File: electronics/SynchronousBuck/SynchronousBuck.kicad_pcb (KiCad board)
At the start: 4 copper layers, 90 x 81 mm, 58 parts, among them J101 Conn_01x02, J102 Conn_01x04_Male, J103 Conn_01x02, J104 Conn_01x02, Q101 BSC070N10NS5, Q102 BSC067N06LS3G, U101 LM5116MH

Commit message: Updated layout and schematic. Added zener diodes to protect output of measurements
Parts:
- removed R102, R109, R110: 1k2, Resistor_SMD:R_0603_1608Metric
- added D102: 5V1, Diode_SMD:D_SOD-123, F.Cu at (126.7, 107.5)
- added D103: 5V1, Diode_SMD:D_SOD-123, F.Cu at (124.3, 97.2)
- added R120: 24k, Resistor_SMD:R_0603_1608Metric, F.Cu at (118.2, 104.0)
- R101: value 24k -> 18k
- moved R101 12.5 mm to (109.1, 121.3)
- turned R111 to 180 degrees
- turned C116 to 270 degrees
- turned C117 to 270 degrees
- turned C120 to 180 degrees
- turned C121 to 90 degrees
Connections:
- C116 pad 1: GND -> /VOUT
- C116 pad 2: /VOUT -> GND
- C117 pad 1: GND -> /VOUT
- C117 pad 2: /VOUT -> GND
- C120 pad 1: GND -> VCC
- C120 pad 2: VCC -> GND
- C121 pad 1: GND -> VCC
- C121 pad 2: VCC -> GND
- R101 pad 1: VCC -> Net-(R101-Pad1)
- R101 pad 2: Net-(R101-Pad2) -> VCC
- R111 pad 1: Net-(R102-Pad2) -> GND
- R111 pad 2: GND -> Net-(R101-Pad1)
- U101 pad 2: Net-(R102-Pad2) -> Net-(R101-Pad1)
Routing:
- net Net-(R101-Pad1): track 0.00 -> 9.76 mm
- net Net-(R102-Pad2): track 8.53 -> 0.00 mm
- net Net-(R102-Pad1): track 5.04 -> 0.00 mm
- net Net-(D103-Pad1): track 5.62 -> 10.1 mm
- net Net-(D102-Pad1): track 6.74 -> 9.19 mm
- net /VOUT: track 106.9 -> 108.7 mm
- net Net-(R109-Pad2): track 1.45 -> 0.00 mm
- net Net-(R101-Pad2): track 1.45 -> 0.00 mm
- net GND: track 22.2 -> 22.3 mm, vias 32 -> 118

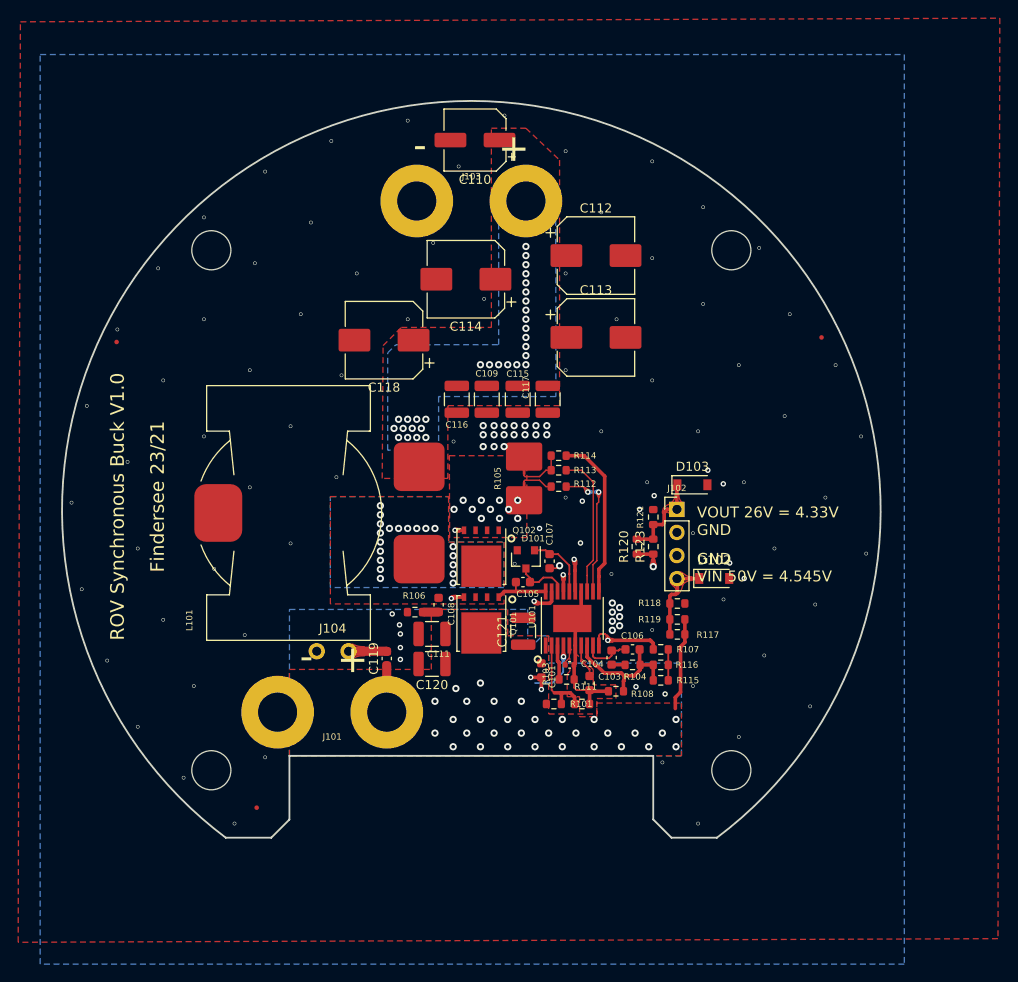
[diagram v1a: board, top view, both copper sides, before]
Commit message: Cleaning silks and moving components
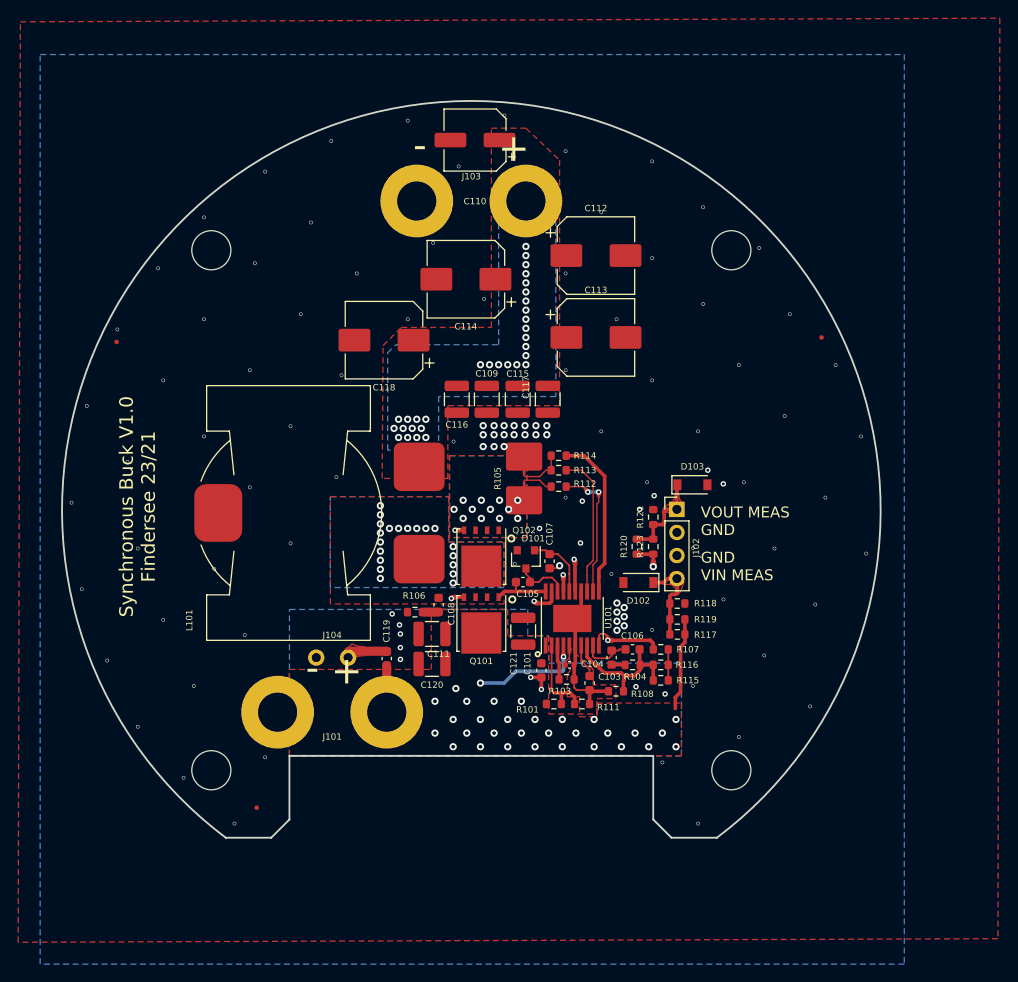
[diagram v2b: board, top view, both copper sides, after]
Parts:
- moved D102 8.35 mm to (118.4, 108.0), turned to 180 degrees
- moved J104 0.70 mm to (84.7, 116.2)
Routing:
- net VCC: track 21.9 -> 27.8 mm
- net Net-(Q102-Pad1): vias 11 -> 12
- net GND: vias 118 -> 116
- added copper zone on B.Cu, net Net-(Q102-Pad1)
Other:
- board text added: "GND VIN MEAS"
- board text added: "Synchronous Buck V1.0 Findersee 23/21"
- board text added: "VOUT MEAS GND"
- board text removed: "Findersee 23/21"
- board text removed: "GND VIN 50V = 4.545V"
- board text removed: "ROV Synchronous Buck V1.0"
- board text removed: "VOUT 26V = 4.33V GND"
